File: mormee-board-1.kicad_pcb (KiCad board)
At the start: 4 copper layers, 40 x 60 mm, 147 parts, among them J1 PDM MEMS Mic, J2 24FLZ-SM2-TB, J3 USB4105-GF-A, J4 Conn_01x02, J5 DM3BT-DSF-PEJS, Q1 AO3401A, SW1 EVQ-PUB02K, SW2 EVQ-PUB02K, U1 W25Q128JVSIQ, U10 MAX17048G+T10, U11 MP2637GR-P, U2 RTL8735BDM-A20-N04, U3 FDS9926A, U4 FT232RNL-REEL, U5 RT8097AHGE, U6 RT8097AHGE, U7 RT9080-28GJ5, U8 RT9080-18GJ5, U9 RT9080-12GJ5

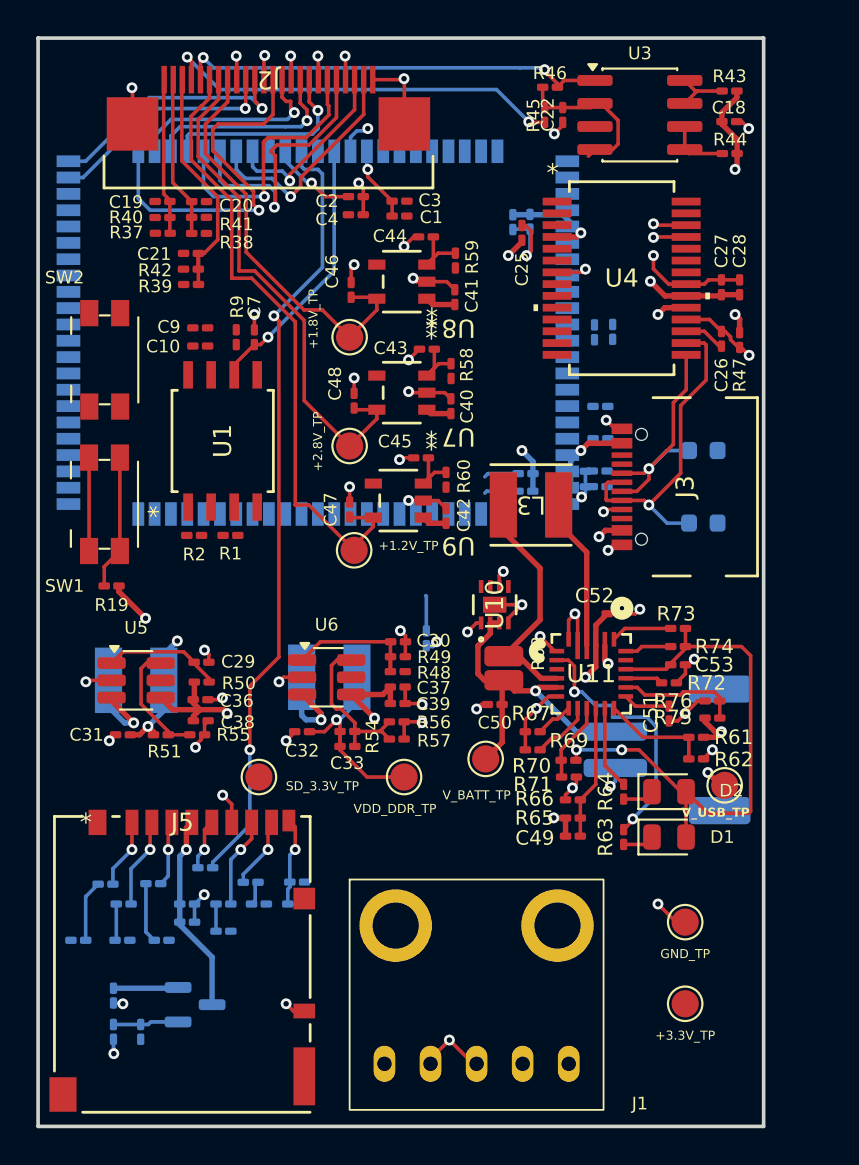
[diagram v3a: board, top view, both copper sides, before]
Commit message: Most signals routed. Just need power plane clean up and final checks. Almost there, but WIP
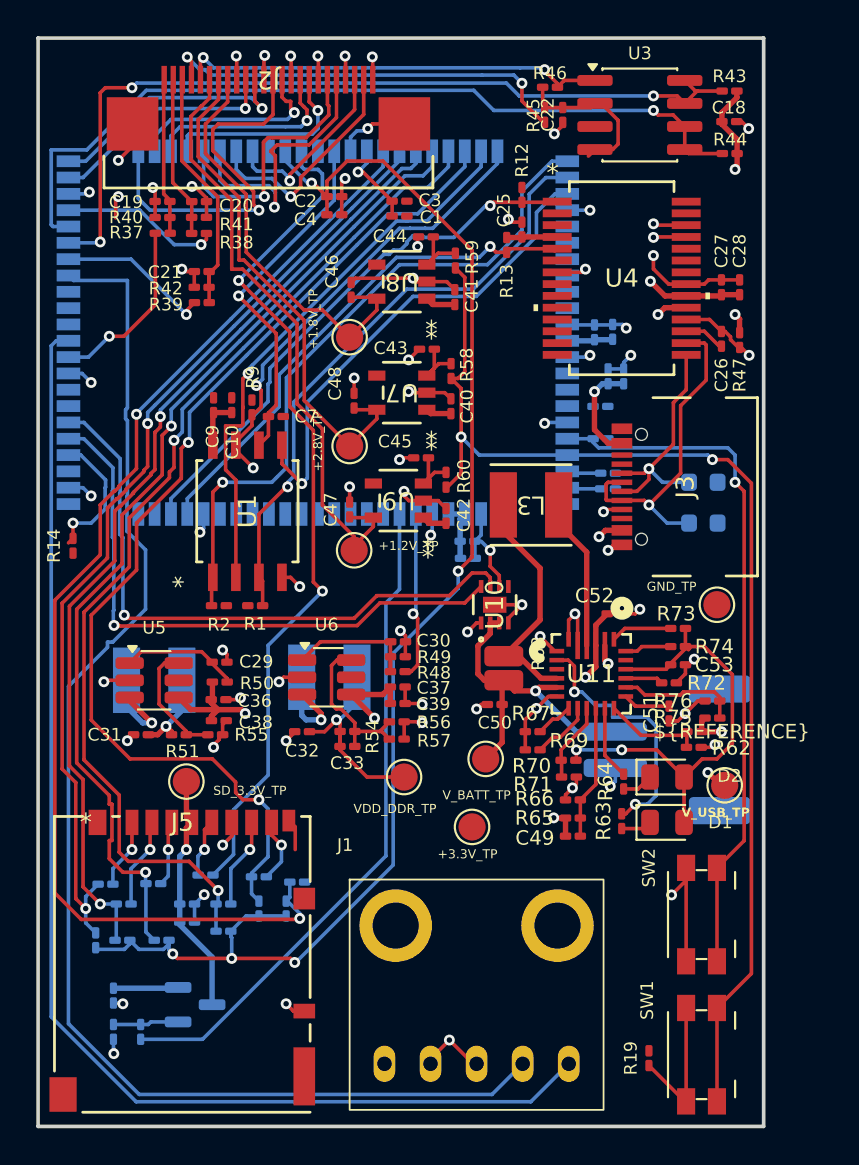
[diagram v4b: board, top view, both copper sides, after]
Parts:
- R12, R13, R14: moved to F.Cu
- moved SW2 44.9 mm to (105.9, 89.1), turned to -90 degrees
- moved SW1 44.8 mm to (105.9, 96.8), turned to -90 degrees
- moved R19 39.4 mm to (103.0, 97.0), turned to -90 degrees
- moved R14 20.1 mm to (71.2, 68.8)
- moved C11 18.7 mm to (93.0, 69.4), turned to 0 degrees
- moved C12 17.9 mm to (93.0, 68.5), turned to 0 degrees
- moved TP9 17.6 mm to (106.8, 72.0)
- moved R12 16.3 mm to (96.0, 49.4), turned to -90 degrees
- moved TP1 15.3 mm to (93.2, 84.2)
- moved R13 12.6 mm to (95.2, 52.2), turned to -90 degrees
- moved C24 6.59 mm to (101.6, 59.4), turned to 90 degrees
- moved C23 5.49 mm to (100.8, 59.4), turned to 90 degrees
- moved C7 4.53 mm to (82.4, 61.6), turned to 0 degrees
- moved C9 4.33 mm to (79.0, 61.0), turned to 90 degrees
- moved R1 4.11 mm to (81.3, 72.1)
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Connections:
- U2 pad 7: DS_D2 -> SD_D2
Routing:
- net DMIC_CLK: track 0.00 -> 74.2 mm
- net VDIO_SD: track 4.82 -> 76.9 mm, vias 1 -> 5
- net DMIC_DATA: track 0.00 -> 69.4 mm
- net SD_CD: track 4.91 -> 66.7 mm, vias 1 -> 2
- net SEN_PWR_EN: track 5.15 -> 65.4 mm, vias 0 -> 2
- net SD_D1: track 1.34 -> 58.6 mm, vias 0 -> 2
- net SD_D0: track 1.50 -> 57.2 mm, vias 0 -> 2
- net SD_CMD: track 3.31 -> 55.0 mm, vias 0 -> 2
- net SD_D3: track 2.03 -> 53.3 mm, vias 0 -> 2
- net SD_D2: track 3.38 -> 52.7 mm, vias 0 -> 2
- net SEN_SDA: track 3.27 -> 46.2 mm, vias 0 -> 3
- net SEN_SCL: track 3.43 -> 45.7 mm, vias 0 -> 1
- net /RTL9835B/CHIP_EN: track 0.00 -> 38.5 mm, vias 0 -> 1
- net /RTL9835B/FLASH_CS: track 0.00 -> 37.6 mm, vias 0 -> 1
- net SD_PWR_EN: track 0.00 -> 36.9 mm
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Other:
- board text added: "${REFERENCE}"

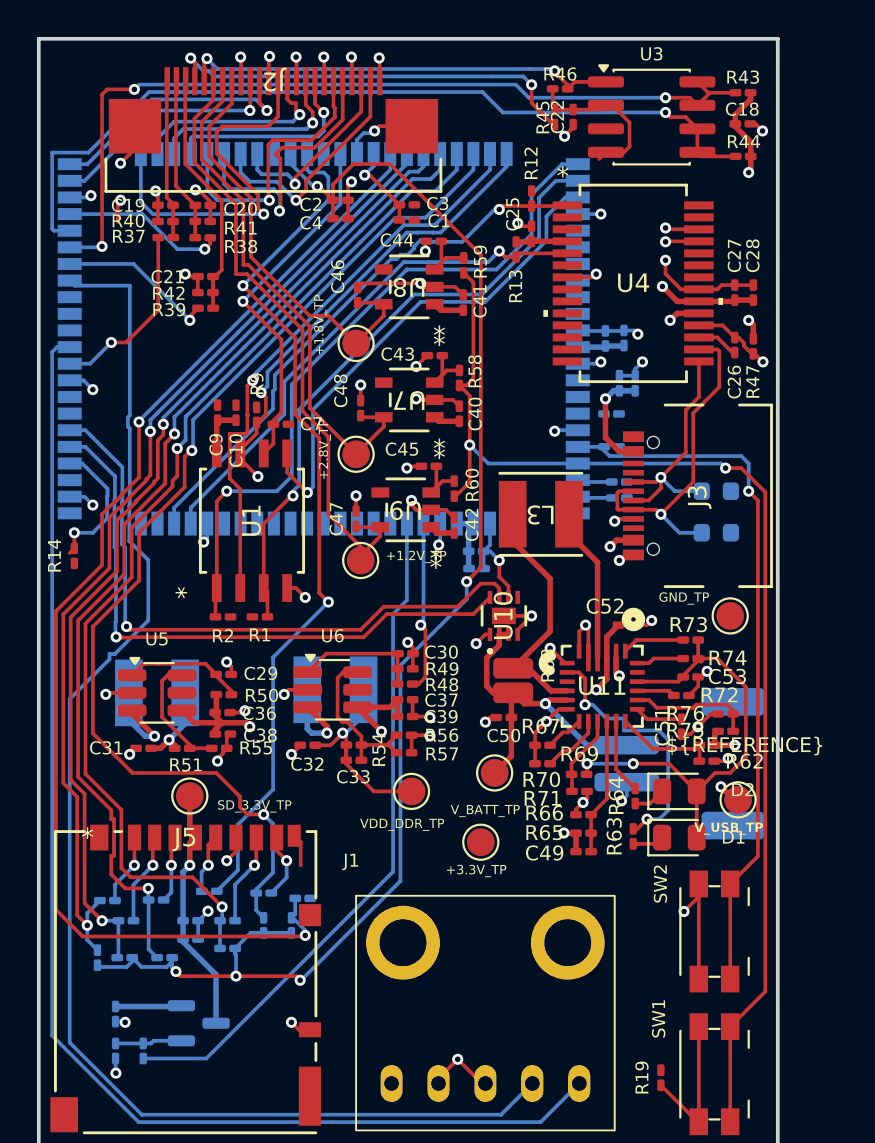
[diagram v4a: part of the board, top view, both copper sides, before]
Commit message: All nets seem to be routed. Checkingo
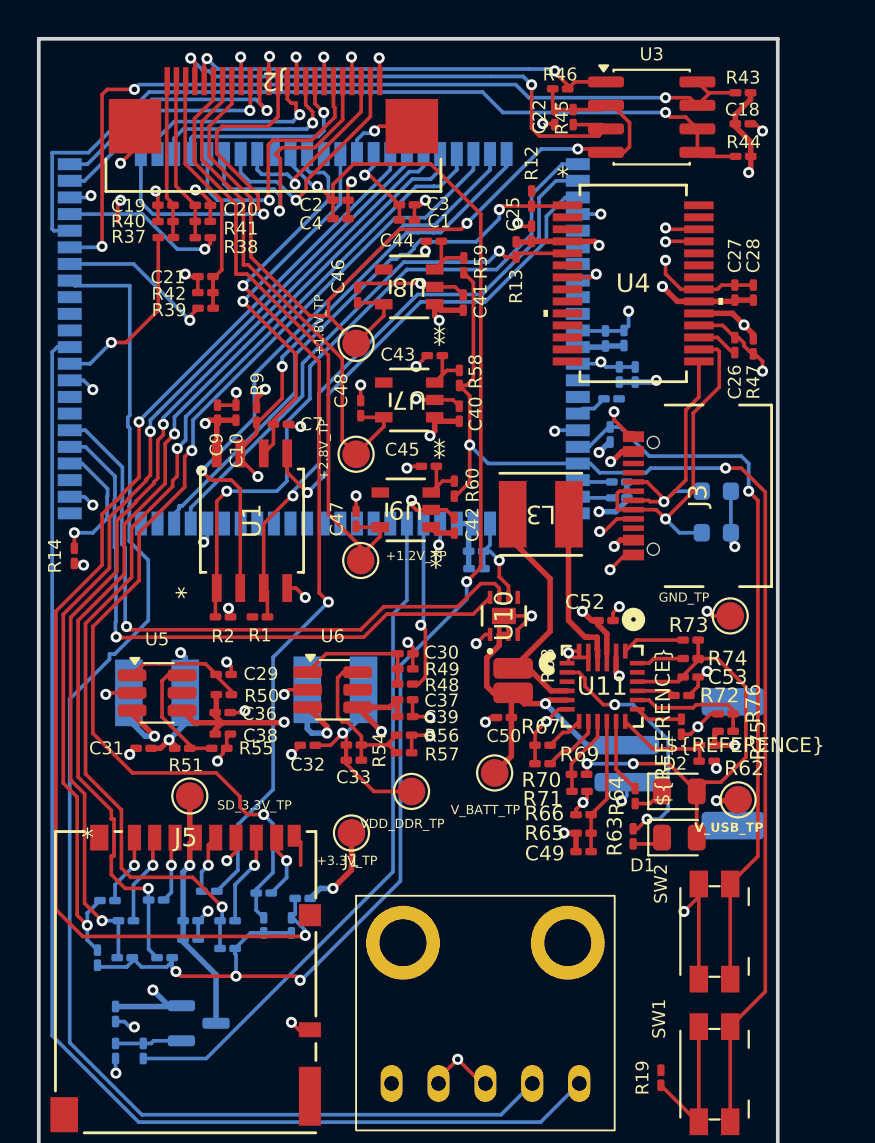
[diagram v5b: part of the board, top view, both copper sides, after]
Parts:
- moved TP1 7.02 mm to (86.2, 83.8)
- moved C52 1.14 mm to (100.0, 72.2)
- moved C22 1.00 mm to (97.2, 45.0)
- moved R45 1.00 mm to (98.2, 45.0)
- moved C5 0.82 mm to (100.3, 60.2)
- moved R15 0.67 mm to (100.2, 62.2), turned to 90 degrees
- moved C23 0.48 mm to (100.8, 58.9)
- moved C24 0.48 mm to (101.6, 58.9)
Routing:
- net +3.3V: track 33.7 -> 53.2 mm, vias 3 -> 15
- net SEN_1V8: track 31.7 -> 50.5 mm, vias 0 -> 2
- net GND: track 131.5 -> 142.3 mm, vias 72 -> 76
- net /SD CARD /Vidio / Audio / USB/SCL: track 23.1 -> 29.0 mm
- net Net-(U2-AOUT_LP): track 0.00 -> 1.75 mm
- net V_USB: track 14.2 -> 12.5 mm
- net /RTL9835B/FLASH_D1: track 31.1 -> 32.5 mm
- net VDIO_SD: track 76.9 -> 78.2 mm
- net Net-(U11-*CHG): track 14.3 -> 13.4 mm
- net /Debug Interface/USB_P: track 13.7 -> 14.6 mm
- net +5V: track 19.8 -> 20.6 mm
- net /RTL9835B/CHIP_EN: track 38.5 -> 39.2 mm
- net /RTL9835B/FLASH_CLK: track 19.6 -> 20.3 mm

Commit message: Board is fully routed
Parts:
- J4: value Conn_01x02 -> S2B-PH-SM4-TB_LF__SN_; footprint Connector_JST:JST_PH_S2B-PH-SM4-TB_1x02-1MP_P2.00mm_Horizontal -> S2B-PH-SM4-TB_LF__SN_:JST_S2B-PH-SM4-TB_LF__SN_
- R68: value 20m -> 20m - WSL1206R0200FEA; footprint Resistor_SMD:R_0508_1220Metric_Pad1.12x2.15mm_HandSolder -> Resistor_SMD:R_1206_3216Metric
- moved J4 2.50 mm to (101.5, 80.0)
- moved SW1 1.50 mm to (107.4, 96.8)
- moved SW2 1.50 mm to (107.4, 89.1)
- moved TP8 0.88 mm to (93.7, 79.7)
- moved R35 0.87 mm to (75.3, 90.5), turned to 90 degrees
- moved R68 0.53 mm to (94.5, 75.2), turned to 0 degrees
- moved C50 0.38 mm to (94.2, 77.7)
- moved R34 0.22 mm to (73.8, 90.5), turned to 90 degrees
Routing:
- net VDD_DDR: track 17.4 -> 52.8 mm, vias 2 -> 3
- net +5V: track 20.6 -> 37.8 mm, vias 4 -> 6
- net +3.3V: track 53.2 -> 67.0 mm, vias 15 -> 16
- net GND: track 142.3 -> 151.2 mm, vias 76 -> 79
- net MDN1: track 14.8 -> 17.6 mm
- net SD_CD: track 66.7 -> 68.6 mm, vias 2 -> 3
- net Net-(SW1-B): track 8.02 -> 9.54 mm
- net MDN2: track 20.6 -> 22.0 mm
- net /Battery/L3: track 13.4 -> 12.0 mm
- net DMIC_CLK: track 74.2 -> 73.2 mm
- net SD_CLK: track 47.1 -> 46.2 mm
- net SD_CMD: track 55.0 -> 54.1 mm
- net VDIO_SD: track 78.2 -> 79.1 mm
- net V_BATT: track 18.5 -> 17.9 mm
- net /RTL9835B/FLASH_D2: track 33.5 -> 34.1 mm
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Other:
- board text removed: "${REFERENCE}"

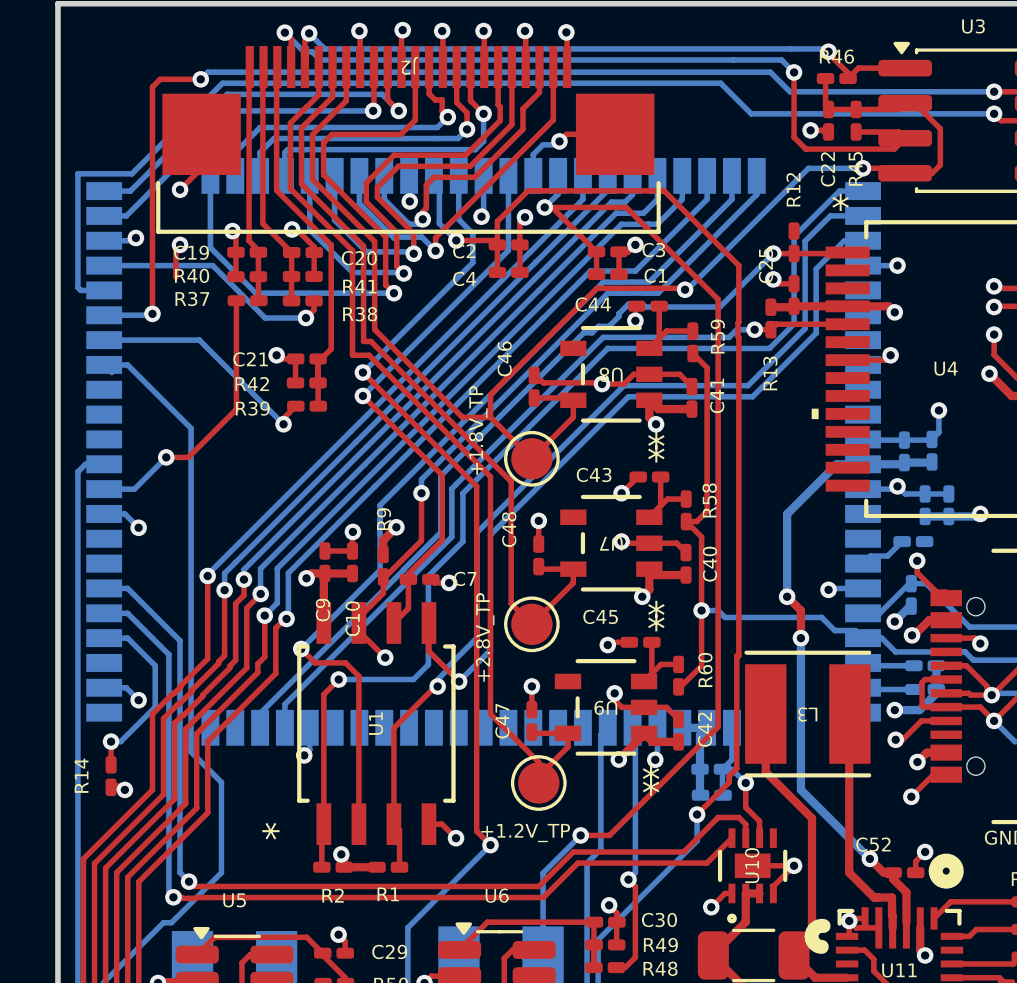
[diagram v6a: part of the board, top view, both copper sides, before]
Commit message: Added text and logo
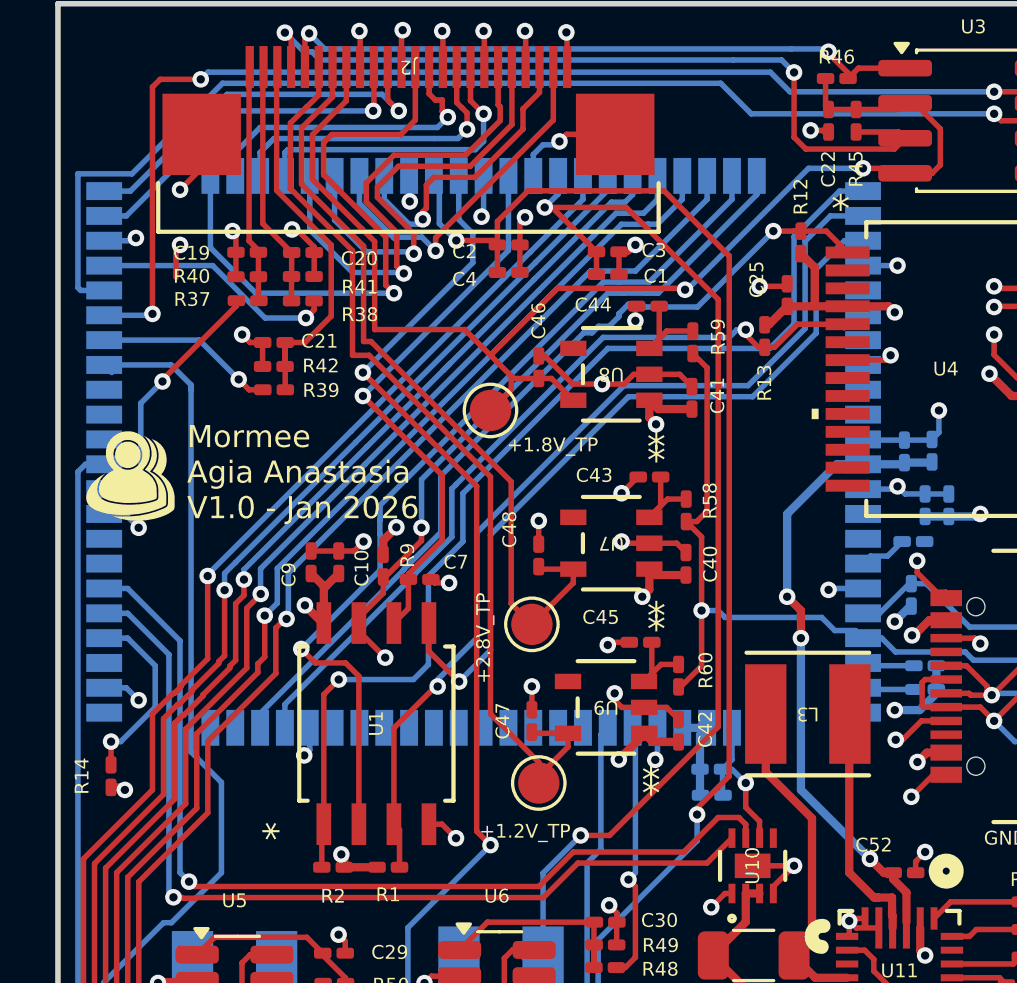
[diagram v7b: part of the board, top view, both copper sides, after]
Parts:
- moved TP3 2.30 mm to (85.0, 55.5)
- moved C21 1.33 mm to (77.2, 53.0)
- moved R39 1.33 mm to (77.2, 54.8)
- moved R42 1.33 mm to (77.1, 53.9)
- moved C46 0.73 mm to (86.8, 53.9)
- moved R13 0.68 mm to (94.9, 52.8)
- moved C10 0.50 mm to (79.5, 61.0)
- moved C9 0.50 mm to (78.5, 61.0)
- moved C25 0.25 mm to (95.8, 51.3)
- moved R12 0.25 mm to (96.2, 49.4), turned to 90 degrees
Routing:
- net SEN_1V8: track 50.6 -> 47.1 mm
- net +3.3V: track 67.0 -> 69.6 mm
- net SEN_SYSCLK: track 8.60 -> 6.50 mm
- net DMIC_CLK: track 73.2 -> 74.2 mm
- net GND: track 151.2 -> 152.2 mm
- net CH_UART_TX: track 30.1 -> 30.7 mm
- net CH_UART_RX: track 28.2 -> 28.8 mm
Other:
- board text added: "Mormee Agia Anastasia V1.0 - Jan 2026"

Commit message: I think I'm done. Fingers crossed.
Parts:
- removed J1: PDM MEMS Mic, Adafruit:Adafruit MEMS 3492
- added C17: 0.1uF, Capacitor_SMD:C_0201_0603Metric_Pad0.64x0.40mm_HandSolder, F.Cu at (101.8, 99.5)
- added C34: 1uF, Capacitor_SMD:C_0201_0603Metric_Pad0.64x0.40mm_HandSolder, F.Cu at (99.8, 99.5)
- added C35: 0.1uF, Capacitor_SMD:C_0201_0603Metric_Pad0.64x0.40mm_HandSolder, F.Cu at (77.0, 99.2)
- added C54: 1uF, Capacitor_SMD:C_0201_0603Metric_Pad0.64x0.40mm_HandSolder, F.Cu at (79.1, 99.2)
- added M1: IMP34DT05TR, IMP34DT05TR:IMP34DT05TR, F.Cu at (78.0, 95.5)
- added M2: IMP34DT05TR, IMP34DT05TR:IMP34DT05TR, F.Cu at (100.8, 95.5)
- moved R28 12.0 mm to (93.5, 87.2), turned to 90 degrees
- moved R29 11.8 mm to (95.2, 89.0), turned to 90 degrees
- moved R27 11.7 mm to (91.2, 88.0), turned to 90 degrees
- moved R31 11.7 mm to (91.2, 90.5), turned to 90 degrees
- moved R24 11.3 mm to (86.9, 88.5)
- moved R23 11.3 mm to (85.3, 89.2)
- moved J5 11.3 mm to (88.5, 92.1)
- moved R22 11.3 mm to (84.3, 87.7)
- moved C13 11.3 mm to (88.8, 88.8)
- moved C14 11.3 mm to (88.8, 89.8)
- moved R32 11.3 mm to (92.8, 89.0)
- moved R33 11.3 mm to (83.8, 90.8)
- moved R34 11.3 mm to (85.0, 90.8)
- moved R35 11.3 mm to (86.5, 90.7)
- moved R36 11.3 mm to (94.3, 89.0)
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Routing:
- net GND: track 152.2 -> 167.2 mm, vias 79 -> 84
- net SD_D0: track 57.2 -> 69.6 mm
- net SD_D1: track 58.6 -> 70.2 mm
- net SD_D2: track 52.7 -> 64.0 mm
- net SD_D3: track 53.3 -> 64.6 mm
- net SD_CMD: track 54.1 -> 65.0 mm
- net SD_CD: track 68.6 -> 79.2 mm
- net VDIO_SD: track 78.8 -> 68.5 mm, vias 5 -> 4
- net SD_3V3: track 13.4 -> 19.4 mm
- net DMIC_CLK: track 74.2 -> 78.0 mm, vias 0 -> 2
- net +3.3V: track 69.6 -> 65.9 mm, vias 16 -> 23
- net SD_CLK: track 46.2 -> 49.4 mm
- net Net-(SW1-B): track 9.54 -> 7.33 mm
- net SD_PWR_EN: track 36.9 -> 34.7 mm
- net DMIC_DATA: track 69.4 -> 70.8 mm, vias 0 -> 2
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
